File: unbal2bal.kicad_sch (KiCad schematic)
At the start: 35 parts, among them J1 RCJ-041, J2 NMJ6HFD2, J3 Mini-DIN-3, J4 Mini-DIN-4, U1 LM4562

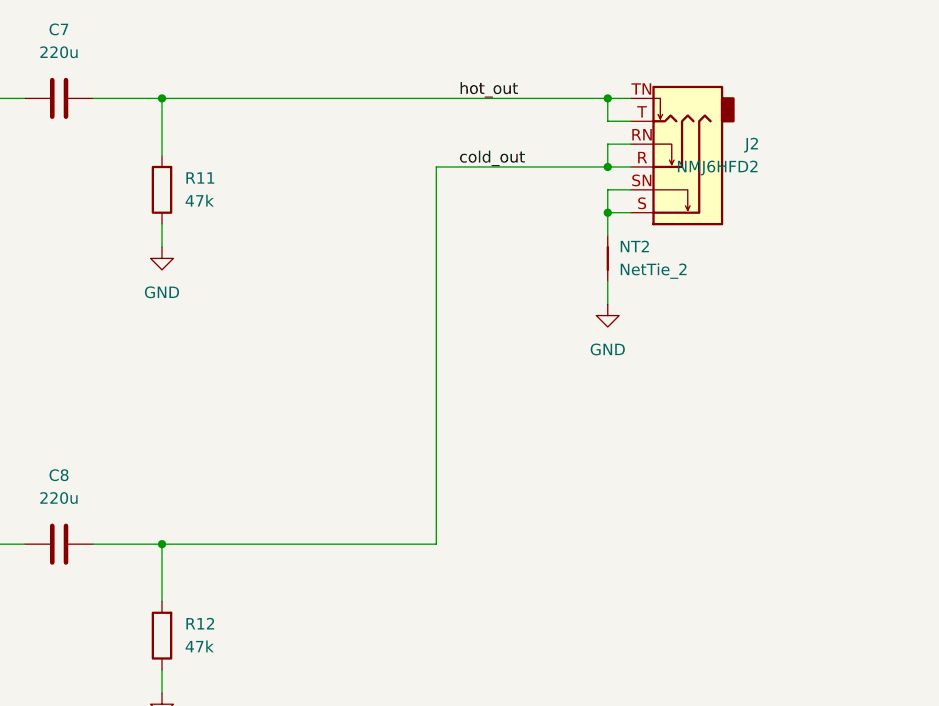
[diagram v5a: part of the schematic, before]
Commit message: change to lower profile 1/4in jack
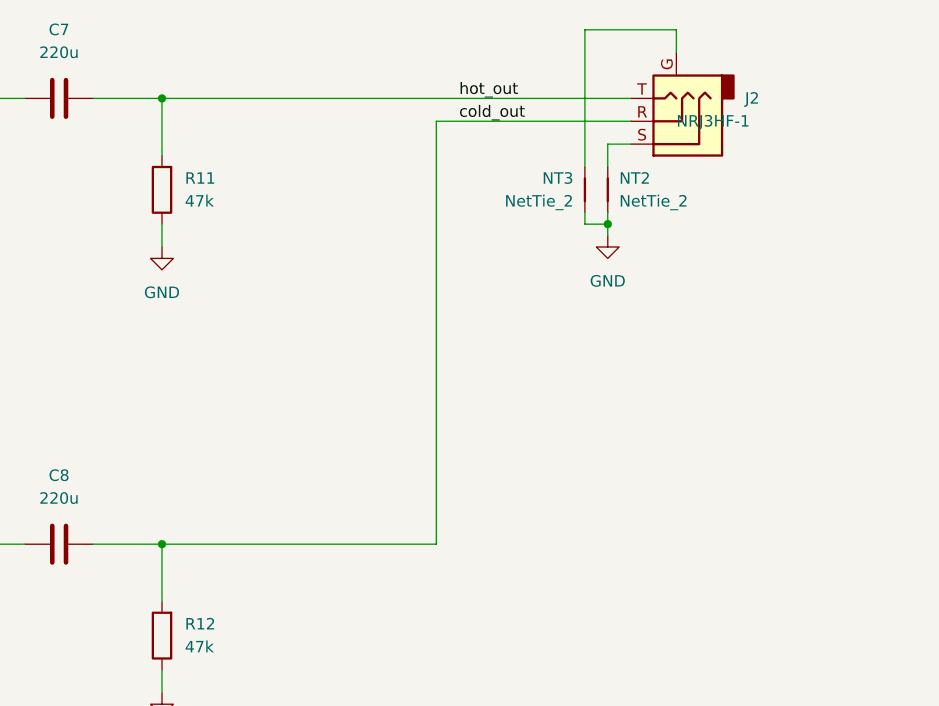
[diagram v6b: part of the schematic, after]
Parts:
- added NT3: NetTie_2, NetTie:NetTie-2_SMD_Pad0.5mm, symbol Device:NetTie_2
- J2: value NMJ6HFD2 -> NRJ3HF-1; footprint Connector_Audio:Jack_6.35mm_Neutrik_NMJ6HFD2_Horizontal -> Connector_Audio:Jack_6.35mm_Neutrik_NRJ3HF-1_Horizontal; symbol Connector:AudioJack3_Switch -> Connector:AudioJack3_Ground; Manufacturer PN NMJ6HFD2 -> NRJ3HF-1
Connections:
- net GND: now also NT3.2
- net cold_out: no longer J2.RN
- net hot_out: no longer J2.TN
- net at J2.S, NT2.1: no longer J2.SN
- new net: J2.G, NT3.1
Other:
- moved on the sheet: NT2

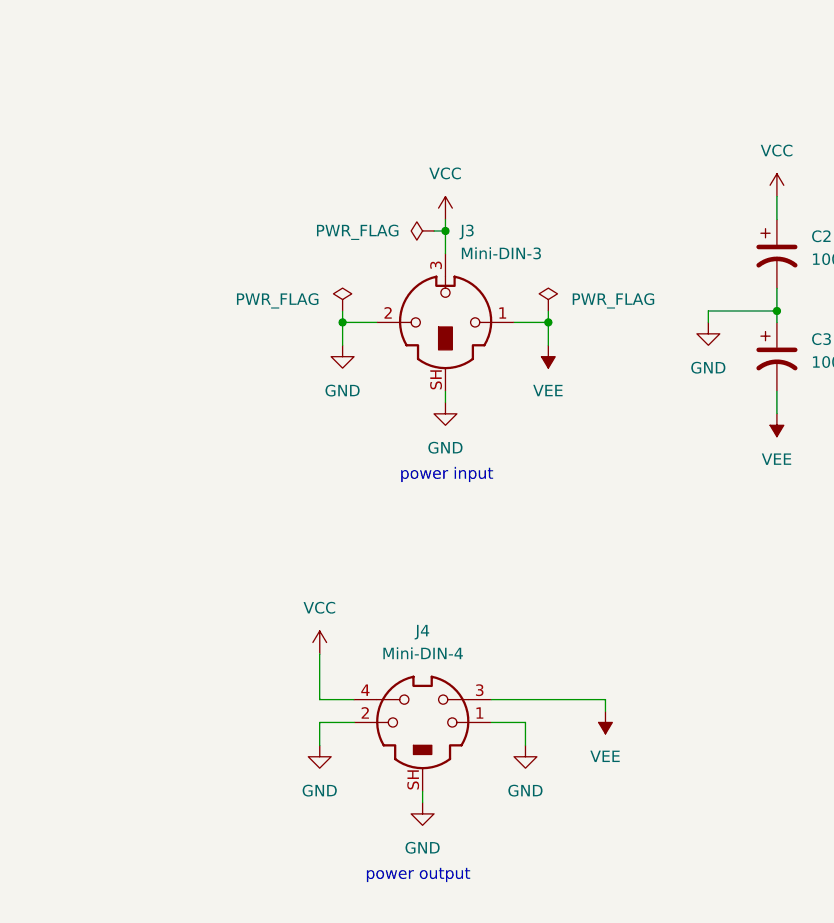
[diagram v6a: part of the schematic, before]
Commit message: switch to power DIN connectors on main board
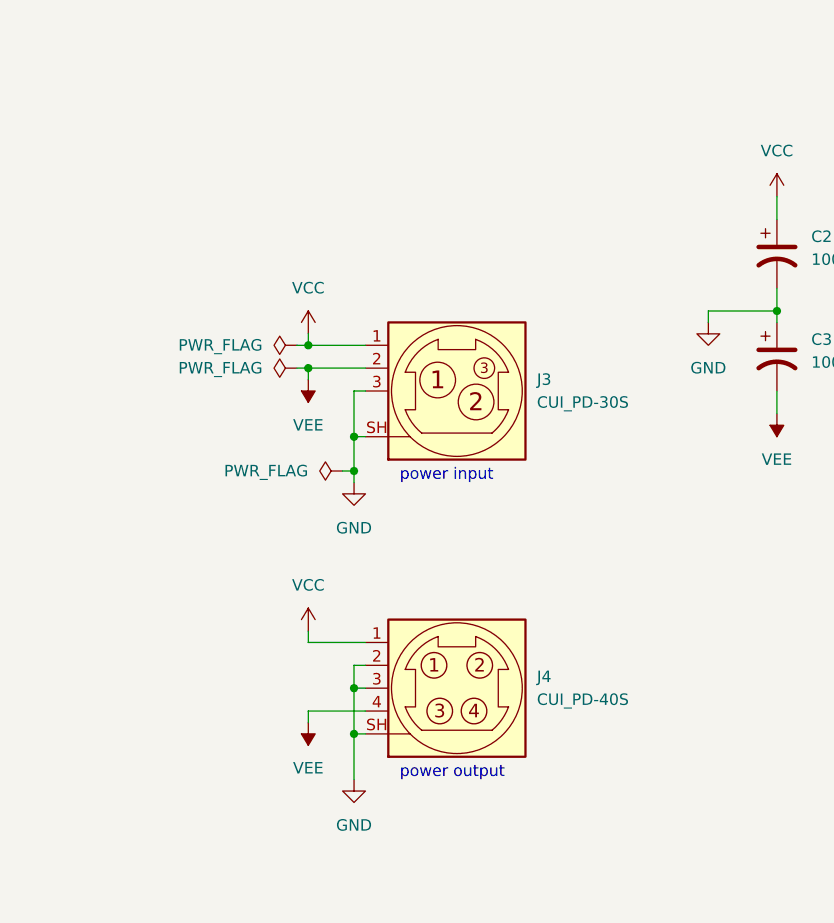
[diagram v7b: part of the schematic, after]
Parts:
- removed J3: Mini-DIN-3, Connector_Mini_DIN_gkeeth:Mini-DIN_Kycon_KMDGX-3S-BS_Horizontal, symbol Connector_gkeeth:Mini-DIN-3_Shielded
- removed J4: Mini-DIN-4, Connector_Mini_DIN_gkeeth:Mini-DIN_Kycon_KMDGX-4S-BS_Horizontal, symbol Connector_gkeeth:Mini-DIN-4_Shielded
- added J3: CUI_PD-30S, Connector_Mini_DIN_gkeeth:Power-DIN_CUI_PD-30S_Horizontal, symbol Connector_gkeeth:CUI_PD-30S
- added J4: CUI_PD-40S, Connector_Mini_DIN_gkeeth:Power-DIN_CUI_PD-40S_Horizontal, symbol Connector_gkeeth:CUI_PD-40S
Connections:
- net GND: now also J3.3, J3.SH (Shield), J4.2, J4.3, J4.SH (Shield)
- net VCC: now also J3.1, J4.1
- net VEE: now also J3.2, J4.4 (Shield)
